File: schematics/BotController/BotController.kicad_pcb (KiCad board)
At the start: 2 copper layers, 29 parts, among them IC1 ATMEGA644A-P, P1 UM2102 - UART2USB, P10 Stepper Upperarm, P11 Stepper Shoulder, P2 Herkulex Servo, P3 Encoder Socket 0, P4 Encoder Socket, P5 Stepper 1 WristTurn, P6 POWER uC, P7 POWER_SERVO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

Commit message: no message
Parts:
- AVR1: footprint Pin_Headers:Pin_Header_Straight_2x03 -> BotController:AVR-ISP-6
- R4: footprint Discret:R4 -> Discret:R5
- X1: footprint Oscillators:OSC_DIP8 -> BotController:OSC_DIP14
- moved R4 128.3 mm to (217.2, 138.4), turned to 90 degrees
- moved R3 110.8 mm to (221.0, 139.7), turned to 90 degrees
- moved R1 64.1 mm to (171.4, 134.6), turned to 180 degrees
- moved C16 53.4 mm to (171.4, 127.0), turned to 180 degrees
- moved C15 52.3 mm to (146.1, 132.1), turned to 90 degrees
- moved P7 50.8 mm to (128.3, 106.7), turned to 90 degrees
- moved P2 42.0 mm to (232.4, 127.0), turned to 270 degrees
- moved D3 38.1 mm to (174.0, 144.8), turned to 180 degrees
- moved P11 36.9 mm to (224.8, 116.8), turned to 90 degrees
- moved P3 30.3 mm to (224.8, 137.2), turned to 90 degrees
- moved X1 29.0 mm to (172.7, 110.5), turned to 270 degrees
- moved D1 25.7 mm to (149.9, 144.8)
- moved P10 23.0 mm to (224.8, 109.2), turned to 90 degrees
- moved P1 20.5 mm to (170.2, 111.8)
- moved AVR1 18.8 mm to (189.2, 109.2)
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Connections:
- net Net-(IC1-Pad13) renamed /TAL
- IC1 pad 18: /En5 -> Net-(IC1-Pad18)
- IC1 pad 21: /EN4 -> /En5
- IC1 pad 23: /SCK -> /SDA
- IC1 pad 26: /EN3 -> /EN4
- IC1 pad 28: /DIR2 -> /DIR3
- IC1 pad 29: /RST -> Net-(IC1-Pad29)
- IC1 pad 33: /CLK2 -> /EN3
- IC1 pad 34: /DIR2 -> /CLK2
- IC1 pad 35: /EN2 -> /DIR2
- IC1 pad 36: Net-(IC1-Pad36) -> /EN2
- P3 pad 3: /SCK -> /SDA
- P4 pad 3: /SCK -> /SDA
- P9 pad 2: /DIR2 -> /DIR3
- R4 pad 2: /SCK -> /SDA

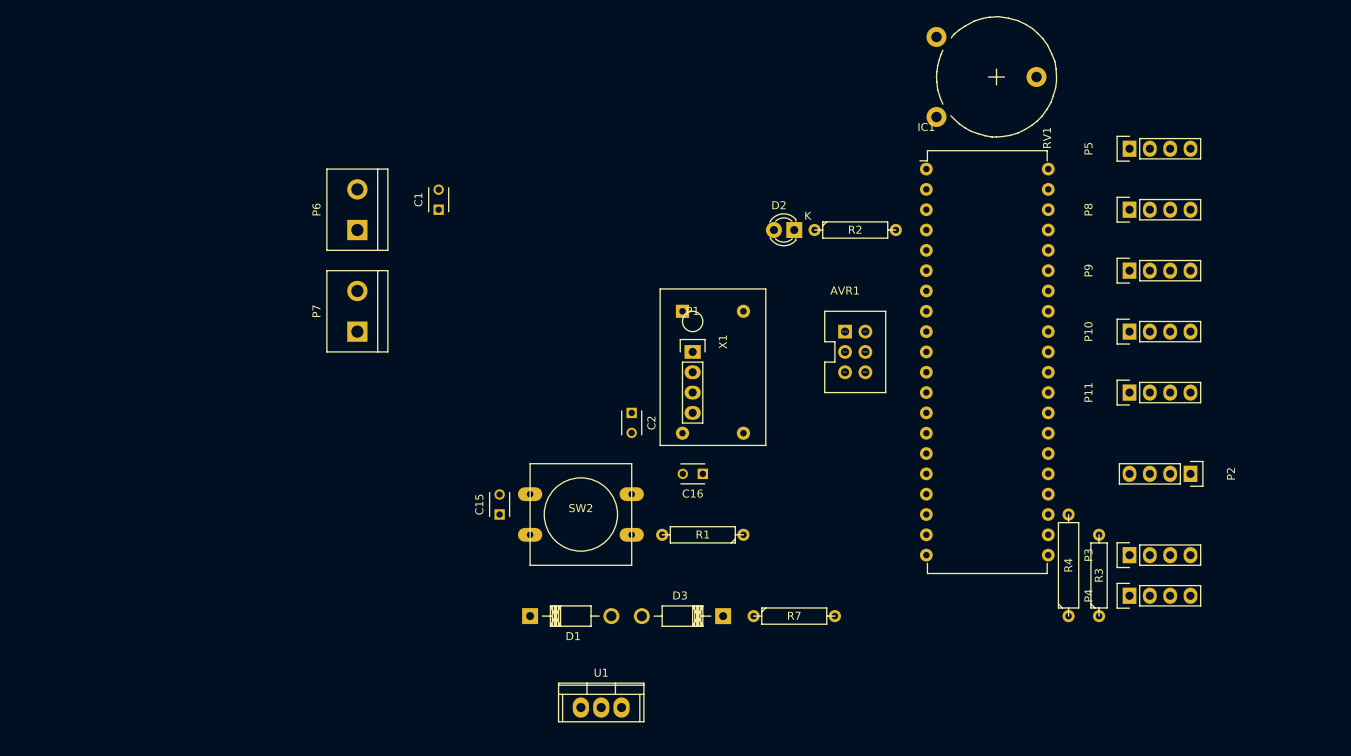
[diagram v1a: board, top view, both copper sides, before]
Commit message: beide Servos angesteuert und Handflansch korrigiert
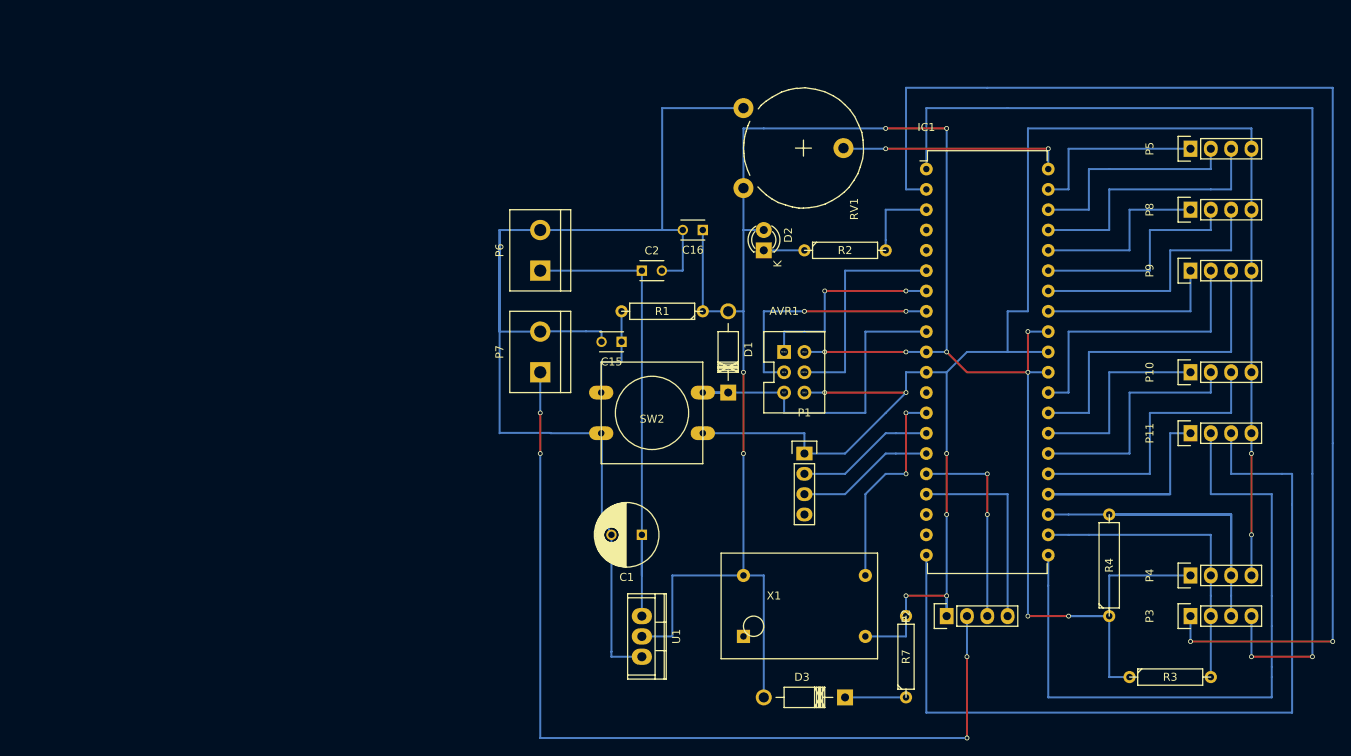
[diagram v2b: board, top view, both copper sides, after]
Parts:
- C1: footprint Capacitors_ThroughHole:C_Disc_D3_P2.5 -> Capacitors_ThroughHole:C_Radial_D8_L13_P3.8
- U1: footprint Power_Integrations:TO-220 -> BotController:78XX-TO-220
- moved C1 47.9 mm to (163.8, 134.6), turned to 180 degrees
- moved D1 37.3 mm to (174.6, 116.8), turned to 90 degrees
- moved P2 35.3 mm to (201.9, 144.8), turned to 90 degrees
- moved X1 33.9 mm to (180.3, 143.5), turned to 0 degrees
- moved C16 30.5 mm to (171.4, 96.5)
- moved R1 28.4 mm to (166.4, 106.7)
- moved C15 26.4 mm to (161.3, 110.5), turned to 180 degrees
- moved RV1 25.7 mm to (176.5, 81.3)
- moved P6 23.4 mm to (151.1, 99.1)
- moved P7 23.4 mm to (151.1, 111.8)
- moved P1 18.9 mm to (184.2, 124.5)
- moved D3 18.3 mm to (189.2, 154.9)
- moved C2 17.8 mm to (163.8, 101.6), turned to 0 degrees
- moved R3 15.5 mm to (229.9, 152.4), turned to 0 degrees
- moved SW2 15.5 mm to (165.1, 119.4), turned to 180 degrees
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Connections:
- IC1 pad 19: /CLK5 -> Net-(IC1-Pad19)
- IC1 pad 20: /DIR5 -> /CLK5
- IC1 pad 21: /En5 -> /DIR5
- IC1 pad 24: /CLK4 -> /En5
- IC1 pad 25: /DIR4 -> /CLK4
- IC1 pad 26: /EN4 -> /DIR4
- IC1 pad 27: /CLK3 -> /EN4
- IC1 pad 28: /DIR3 -> /CLK3
- IC1 pad 29: Net-(IC1-Pad29) -> /DIR3
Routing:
- net GNDPWR: track 0.00 -> 395.9 mm, vias 0 -> 8
- net /+5V: track 0.00 -> 274.7 mm, vias 0 -> 11
- net /ConflictEncoderVDD: track 0.00 -> 158.8 mm, vias 0 -> 2
- net /ConflictEncoderGND: track 0.00 -> 137.2 mm, vias 0 -> 2
- net Net-(P2-Pad2): track 0.00 -> 114.3 mm, vias 0 -> 4
- net /CLK5: track 0.00 -> 108.0 mm
- net /DIR5: track 0.00 -> 86.4 mm
- net /SDA: track 0.00 -> 78.7 mm
- net Net-(C1-Pad1): track 0.00 -> 61.0 mm
- net /RST: track 0.00 -> 56.5 mm
- net /En5: track 0.00 -> 55.9 mm
- net /CLK3: track 0.00 -> 40.6 mm
- net /SCl: track 0.00 -> 38.1 mm
- net /CLK4: track 0.00 -> 35.6 mm
- net /DIR3: track 0.00 -> 35.6 mm
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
